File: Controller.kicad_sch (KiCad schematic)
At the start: 0 parts

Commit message: Add files via upload
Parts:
- added C1, C2, C3: 104, symbol Device:C_US
- added C4, C5: 22P, symbol Device:C_US
- added C6, C7: 12P, symbol Device:C_US
- added D4, D5, D6: LED, symbol Device:LED
- added J1: Conn_ARM_JTAG_SWD_20, symbol Connector:Conn_ARM_JTAG_SWD_20
- added J2: Conn_01x05_Pin, symbol Connector:Conn_01x05_Pin
- added J3, J6, J7: Conn_01x04_Pin, symbol Connector:Conn_01x04_Pin
- added J4, J9: Conn_01x02_Pin, symbol Connector:Conn_01x02_Pin
- added J5: Screw_Terminal_01x02, symbol Connector:Screw_Terminal_01x02
- added J8: Conn_01x06_Pin, symbol Connector:Conn_01x06_Pin
- added R1, R12, R2, R3, R4, R5, R6, R7, R8: 10K, symbol Device:R
- added R10, R11, R9: 510R, symbol Device:R
- added SW1, SW2: SW_Push, symbol Switch:SW_Push
- added U1: STM32F407VETx, Package_QFP:LQFP-100_14x14mm_P0.5mm, symbol MCU_ST_STM32F4:STM32F407VETx
- added U2: W25Q16JVSS, Package_SO:SOIC-8_5.3x5.3mm_P1.27mm, symbol Memory_Flash:W25Q16JVSS
- added U3: MAX485E, Package_SO:SOIC-8_3.9x4.9mm_P1.27mm, symbol Interface_UART:MAX485E
- added Y1: 8M, symbol Device:Crystal
- added Y2: 32.768K, symbol Device:Crystal
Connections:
- new net: R7.2, SW1.2, U1.94 (BOOT0)
- new net: R9.1, U1.15 (PC0)
- new net: D4.2 (A), R9.2
- new net: C4.1, R12.1, U1.12 (PH0), Y1.2
- new net: C5.1, R12.2, U1.13 (PH1), Y1.1
- new net: C7.1, U1.8 (PC14), Y2.1
- new net: C6.1, U1.9 (PC15), Y2.2
- new net: J5.1 (Pin_1), U3.6 (A)
- new net: J5.2 (Pin_2), U3.7 (B)
- new net: R10.1, U1.16 (PC1)
- new net: D5.2 (A), R10.2
- new net: U1.10 (VSS), U1.27 (VSS), U1.74 (VSS), U1.99 (VSS)
- new net: R11.1, U1.17 (PC2)
- new net: D6.2 (A), R11.2
- new net  F_CS PA7: R8.2, U2.1 (~{CS})
- new net +3V3: C1.1, C3.1, J1.1 (VTREF), J1.2 (VCC/NC), R1.1, R3.1, R4.1, R5.1, R6.1, R8.1, SW1.1, U2.3 (~{WP}/IO_{2}), U2.7 (~{HOLD}/~{RESET}/IO_{3}), U2.8 (VCC)
- new net +5V: U3.8 (VCC)
- new net 3V3: J2.4 (Pin_4), J3.4 (Pin_4)
- new net F_CS PA7: U1.32 (PA7)
- new net GND: C1.2, C2.2, C3.2, C4.2, C5.2, C6.2, C7.2, D4.1 (K), D5.1 (K), D6.1 (K), J1.10 (GND), J1.12 (GND), J1.14 (GND), J1.16 (GND), J1.18 (GND), J1.20 (GND), J1.4 (GND), J1.6 (GND), J1.8 (GND), J2.5 (Pin_5), J3.3 (Pin_3), J4.1 (Pin_1), R2.1, R7.1, SW2.1, U2.4 (GND), U3.5 (GND)
- new net PA0 (ADC123_IN0): J8.1 (Pin_1), U1.23 (PA0)
- new net PA1(ADC123_IN1): J8.2 (Pin_2), U1.24 (PA1)
- new net PA10(TIM1_CH3): J6.3 (Pin_3), U1.69 (PA10)
- new net PA11(TIM1_CH4): J6.4 (Pin_4), U1.70 (PA11)
- new net PA2(ADC123_IN2): J8.3 (Pin_3), U1.25 (PA2)
- new net PA3(ADC123_IN3): J8.4 (Pin_4), U1.26 (PA3)
- new net PA4(ADC123_IN4): J8.5 (Pin_5), J9.1 (Pin_1), U1.29 (PA4)
- new net PA8(TIM1_CH1): J6.1 (Pin_1), U1.67 (PA8)
- new net PA9(TIM1_CH2): J6.2 (Pin_2), U1.68 (PA9)
- new net PC6 (TIM8_CH1): J7.1 (Pin_1), U1.63 (PC6)
- new net PC7 (TIM8_CH2): J7.2 (Pin_2), U1.64 (PC7)
- new net PC8 (TIM8_CH3): J7.3 (Pin_3), U1.65 (PC8)
- new net PC9 (TIM8_CH4): J7.4 (Pin_4), U1.66 (PC9)
- new net RST: C2.1, J1.15 (~{SRST}), J2.3 (Pin_3), J4.2 (Pin_2), R6.2, SW2.2, U1.14 (NRST)
- new net RX (PA10): J3.2 (Pin_2)
- new net SPI1_MISO PA6: U1.31 (PA6), U2.2 (DO/IO_{1})
- new net SPI1_MOSI PA7: U2.5 (DI/IO_{0})
- new net SPI1_SCK PA5: J8.6 (Pin_6), J9.2 (Pin_2), U1.30 (PA5), U2.6 (CLK)
- new net SWCLK (PA14): J2.2 (Pin_2)
- new net SWDIO (PA13): J2.1 (Pin_1)
- new net TCK: J1.9 (TCK/SWCLK), R2.2, U1.76 (PA14)
- new net TDI: J1.5 (TDI), R4.2, U1.77 (PA15)
- new net TDO: J1.13 (TDO/SWO), R5.2, U1.89 (PB3)
- new net TMS: J1.7 (TMS/SWDIO), R3.2, U1.72 (PA13)
- new net TRST: J1.3 (~{TRST}), R1.2, U1.90 (PB4)
- new net TX (PA9): J3.1 (Pin_1)
- new net Tranciver DE: U1.33 (PC4), U3.3 (DE)
- new net Tranciver RE: U1.18 (PC3), U3.2 (~{RE})
- new net UART RX PA10: U3.4 (DI)
- new net UART TX PA9: U3.1 (RO)
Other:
- note added: "ADC pins"
- note added: "Button and needed circuitry for RESET"
- note added: "DAC pins"
- note added: "JTAG/SWD Debug Interface"
- note added: "Needed Headers for SWD debugging"
- note added: "Needed Headers for UART programming"
- note added: "Needed circuitry for flash"
- note added: "RS485 Tranciver"
- note added: "TIM1 pins"
- note added: "TIM8 pins"

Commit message: Latest updates
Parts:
- removed C1, C3: 104, symbol Device:C_US
- removed C6, C7: 12P, symbol Device:C_US
- removed D4, D5, D6: LED, symbol Device:LED
- removed J1: Conn_ARM_JTAG_SWD_20, symbol Connector:Conn_ARM_JTAG_SWD_20
- removed J2: Conn_01x05_Pin, symbol Connector:Conn_01x05_Pin
- removed J5: Screw_Terminal_01x02, symbol Connector:Screw_Terminal_01x02
- removed J6, J7: Conn_01x04_Pin, symbol Connector:Conn_01x04_Pin
- removed J8: Conn_01x06_Pin, symbol Connector:Conn_01x06_Pin
- removed J9: Conn_01x02_Pin, symbol Connector:Conn_01x02_Pin
- removed R1, R4, R8: 10K, symbol Device:R
- removed R10, R11, R9: 510R, symbol Device:R
- removed SW1: SW_Push, symbol Switch:SW_Push
- removed U2: W25Q16JVSS, Package_SO:SOIC-8_5.3x5.3mm_P1.27mm, symbol Memory_Flash:W25Q16JVSS
- removed U3: MAX485E, Package_SO:SOIC-8_3.9x4.9mm_P1.27mm, symbol Interface_UART:MAX485E
- added C10, C11, C12, C13, C23, C7, C8, C9: 100n, symbol Device:C
- added C14: 4.7u, symbol Device:C
- added C3, C4: 2.2u, symbol Device:C
- added C5, C6: 6.8p, symbol Device:C
- added D1, D2, D3: LED, symbol Device:LED
- added J12: Conn_01x03_Pin, symbol Connector:Conn_01x03_Pin
- added J2: Conn_01x04_Pin, symbol Connector:Conn_01x04_Pin
- added J3, J4: Conn_01x02_Pin, symbol Connector:Conn_01x02_Pin
- added R17, R6: 1k, symbol Device:R
- added U6: TL431M-0.3%-6AF, EasyEDA:SOT-23-3_L2.9-W1.6-P1.90-LS2.8-BR, symbol EasyEDA:TL431M-0.3%-6AF
- C1: renamed from C4; value 22P -> 20p
- C15: renamed from C2; value 104 -> 1u
- C2: renamed from C5; value 22P -> 20p
- R5, R7: value 10K -> 1k
- renumbered J3 to J5, J4 to J6, R12 to R1, R6 to R4, SW2 to SW1
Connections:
- net 3V3 is gone; now on net GND: J5.4 (Pin_4)
- net RX (PA10) is gone; now on net UART1_Rx: J5.2 (Pin_2)
- net TX (PA9) is gone; now on net UART1_Tx: J5.1 (Pin_1)
- net +3V3: now also J5.3 (Pin_3), U1.100 (VDD), U1.11 (VDD), U1.19 (VDD), U1.22 (VDDA), U1.28 (VDD), U1.50 (VDD), U1.75 (VDD), C10.1, C11.1, C12.1, C13.1, C14.1, C7.1, C8.1, C9.1, D1.1 (K), D2.1 (K), D3.1 (K), J12.3 (Pin_3), J2.3 (Pin_3), J3.2 (Pin_2), J4.2 (Pin_2), R17.1; no longer R3.1, R5.1
- net GND: now also R2.2, R3.2, U1.10 (VSS), U1.20 (VSSA), U1.27 (VSS), U1.74 (VSS), U1.99 (VSS), C10.2, C11.2, C12.2, C13.2, C14.2, C23.2, C3.2, C4.2, C5.2, C6.2, C7.2, C8.2, C9.2, J2.4 (Pin_4), U6.3 (A); no longer J5.3 (Pin_3), R2.1, R7.1
- net SWCLK (PA14): now also U1.76 (PA14), J2.2 (Pin_2)
- net SWDIO (PA13): now also U1.72 (PA13), J2.1 (Pin_1)
- net at R7.2: now also D3.2 (A); no longer U1.94 (BOOT0)
- net UserLED1: now reaches U1.15 (PC0)
- net UserLED1: now also R5.1
- net at U1.8 (PC14), Y2.1: now also C5.1
- net at U1.9 (PC15), Y2.2: now also C6.1
- net UserLED2: now reaches U1.16 (PC1)
- net UserLED2: now also R6.1
- net UserLED3: now reaches U1.17 (PC2)
- net UserLED3: now also R7.1
- net VREF: now reaches U1.21 (VREF+)
- net VREF: now also C23.1, J12.2 (Pin_2)
- net BOOT1: now reaches U1.37 (PB2)
- net BOOT1: now also R2.1, J3.1 (Pin_1)
- net at U1.49 (VCAP_1): now also C3.1
- net PB13(TIM1_CH1N): now reaches U1.52 (PB13)
- net PB14(TIM1_CH2N): now reaches U1.53 (PB14)
- net PB15(TIM1_CH3N): now reaches U1.54 (PB15)
- net OTG_FS_DP: now reaches U1.71 (PA12)
- net at U1.73 (VCAP_2): now also C4.1
- net UART1_Tx: now reaches U1.92 (PB6)
- net UART1_Rx: now reaches U1.93 (PB7)
- net CAN1_Rx: now reaches U1.95 (PB8)
- net CAN1_Tx: now reaches U1.96 (PB9)
- net F_CS PA7: no longer names the net of U1.32 (PA7)
- net PA0 (ADC123_IN0): no longer names the net of U1.23 (PA0)
- net PA1(ADC123_IN1): no longer names the net of U1.24 (PA1)
- net PA11(TIM1_CH4) renamed OTG_FS_DM
- net PA2(ADC123_IN2) renamed UART2_Tx
- net PA3(ADC123_IN3) renamed UART2_Rx
- net PA4(ADC123_IN4): no longer names the net of U1.29 (PA4)
- net PC6 (TIM8_CH1): no longer names the net of U1.63 (PC6)
- net PC7 (TIM8_CH2): no longer names the net of U1.64 (PC7)
- net PC8 (TIM8_CH3): no longer names the net of U1.65 (PC8)
- net PC9 (TIM8_CH4): no longer names the net of U1.66 (PC9)
- net RST renamed NRST
- net SPI1_MISO PA6: no longer names the net of U1.31 (PA6)
- net SPI1_SCK PA5: no longer names the net of U1.30 (PA5)
- removed net TCK: R2.2, U1.76 (PA14)
- net TDI: no longer names the net of U1.77 (PA15)
- net TDO: no longer names the net of U1.89 (PB3)
- net TDO: no longer R5.2
- removed net TMS: R3.2, U1.72 (PA13)
- net TRST: no longer names the net of U1.90 (PB4)
- net Tranciver DE: no longer names the net of U1.33 (PC4)
- net Tranciver RE: no longer names the net of U1.18 (PC3)
- new net: D2.2 (A), R6.2
- new net: D1.2 (A), R5.2
- new net BOOT0: J4.1 (Pin_1), R3.1, U1.94 (BOOT0)
- new net VREF_2.5V: J12.1 (Pin_1), R17.2, U6.1 (REF), U6.2 (C)
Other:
- note added: "HSE and LSE circuitry based on https://github.com/AlexanderDev/stm32f4discovery/blob/master/doc/schematics.pdf"
- note added: "Needed Headers for UART programming/Debugging"
- note added: "USER LEDS"
- note removed: "ADC pins"
- note removed: "DAC pins"
- note removed: "JTAG/SWD Debug Interface"
- note removed: "Needed Headers for UART programming"
- note removed: "Needed circuitry for flash"
- note removed: "RS485 Tranciver"
- note removed: "TIM1 pins"
- note removed: "TIM8 pins"
- moved on the sheet: C1, C15, C2, J5, J6, R1, R4, SW1, U1, Y1, Y2

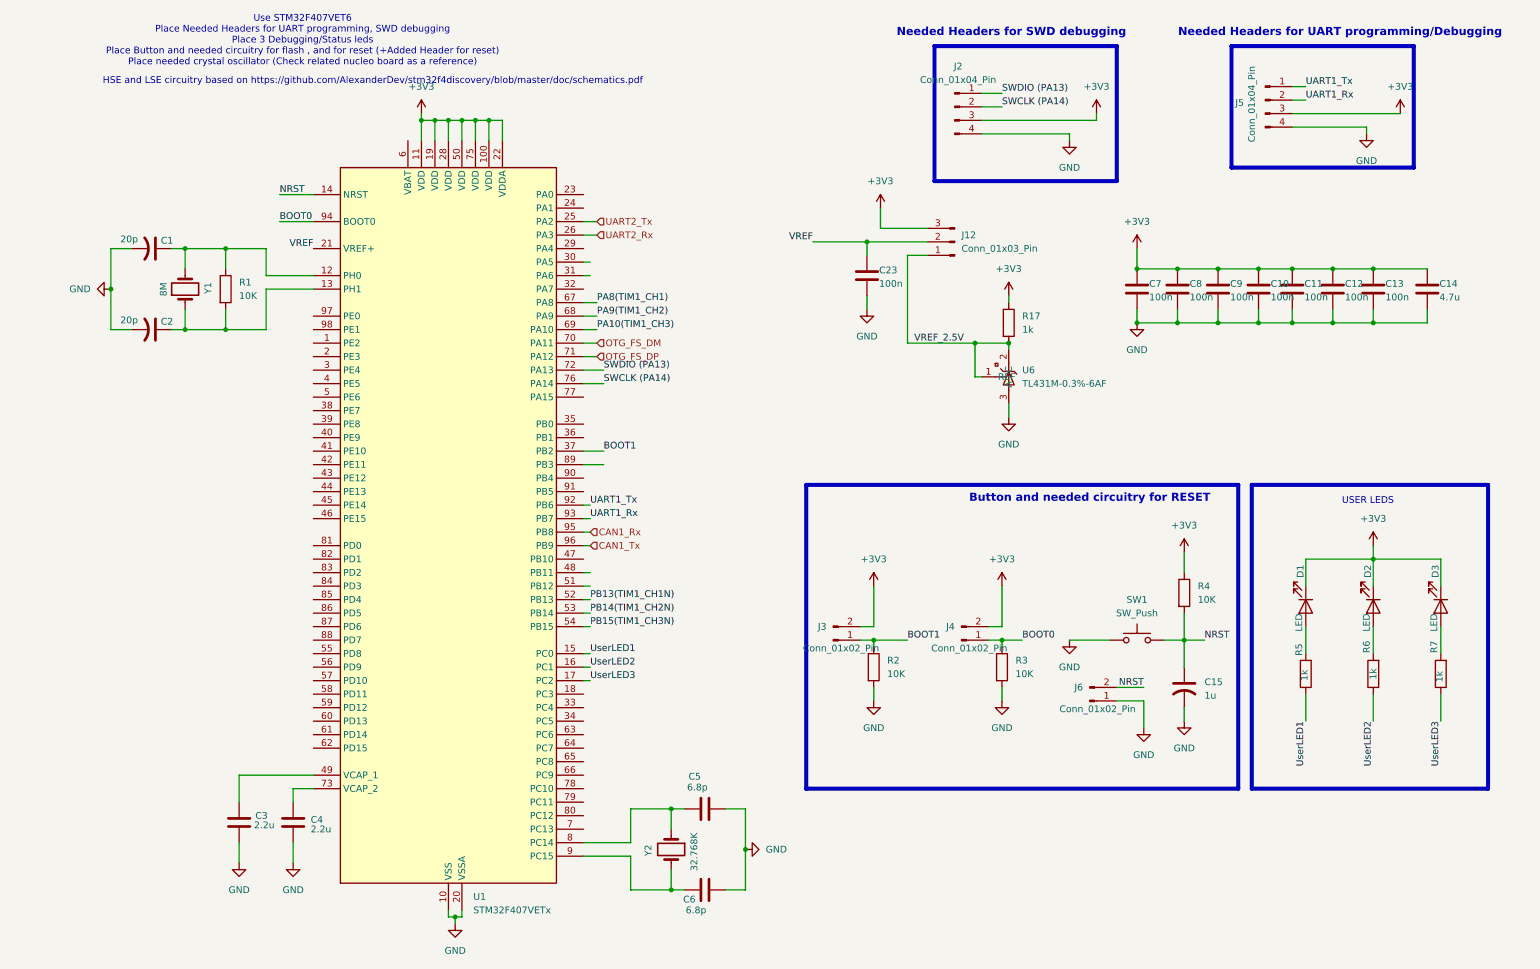
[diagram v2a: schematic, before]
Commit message: Latest changes (added SD , USB , CAN , RS485)
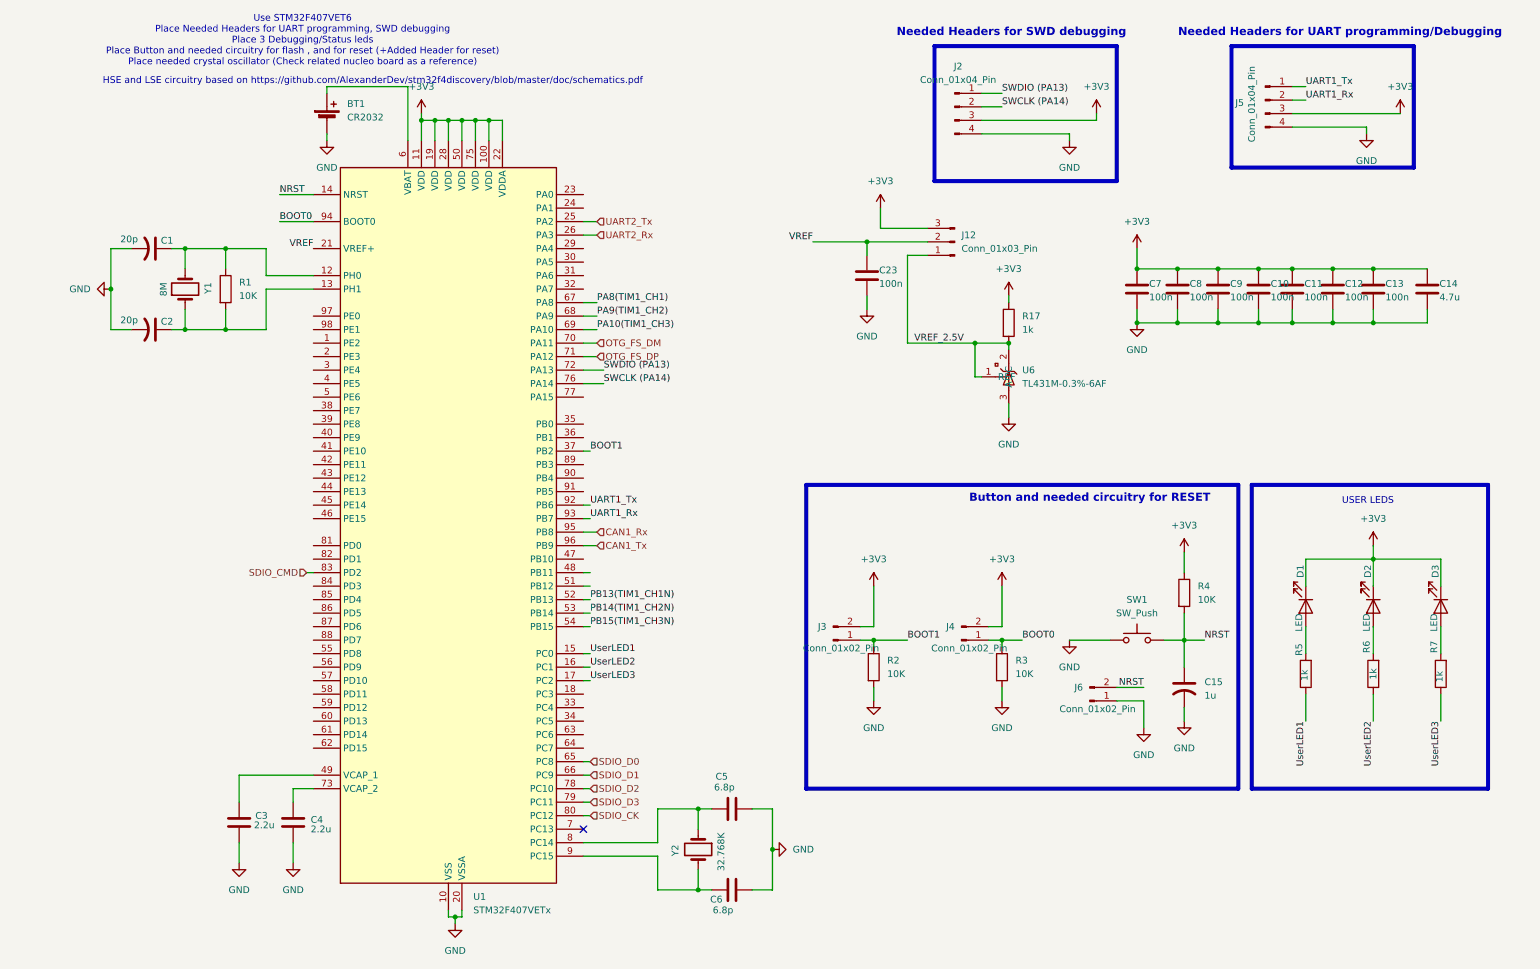
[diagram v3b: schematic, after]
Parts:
- added BT1: CR2032, EasyEDA:BAT_1074, symbol Device:Battery_Cell
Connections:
- net GND: now also BT1.2 (-)
- net at U1.6 (VBAT): now also BT1.1 (+)
- net SDIO_D0: now reaches U1.65 (PC8)
- net SDIO_D1: now reaches U1.66 (PC9)
- net SDIO_D2: now reaches U1.78 (PC10)
- net SDIO_D3: now reaches U1.79 (PC11)
- net SDIO_CK: now reaches U1.80 (PC12)
- net SDIO_CMD: now reaches U1.83 (PD2)
- no-connect marks 0 -> 1
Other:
- moved on the sheet: C5, C6, Y2

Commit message: added Ethernet and SPI interface
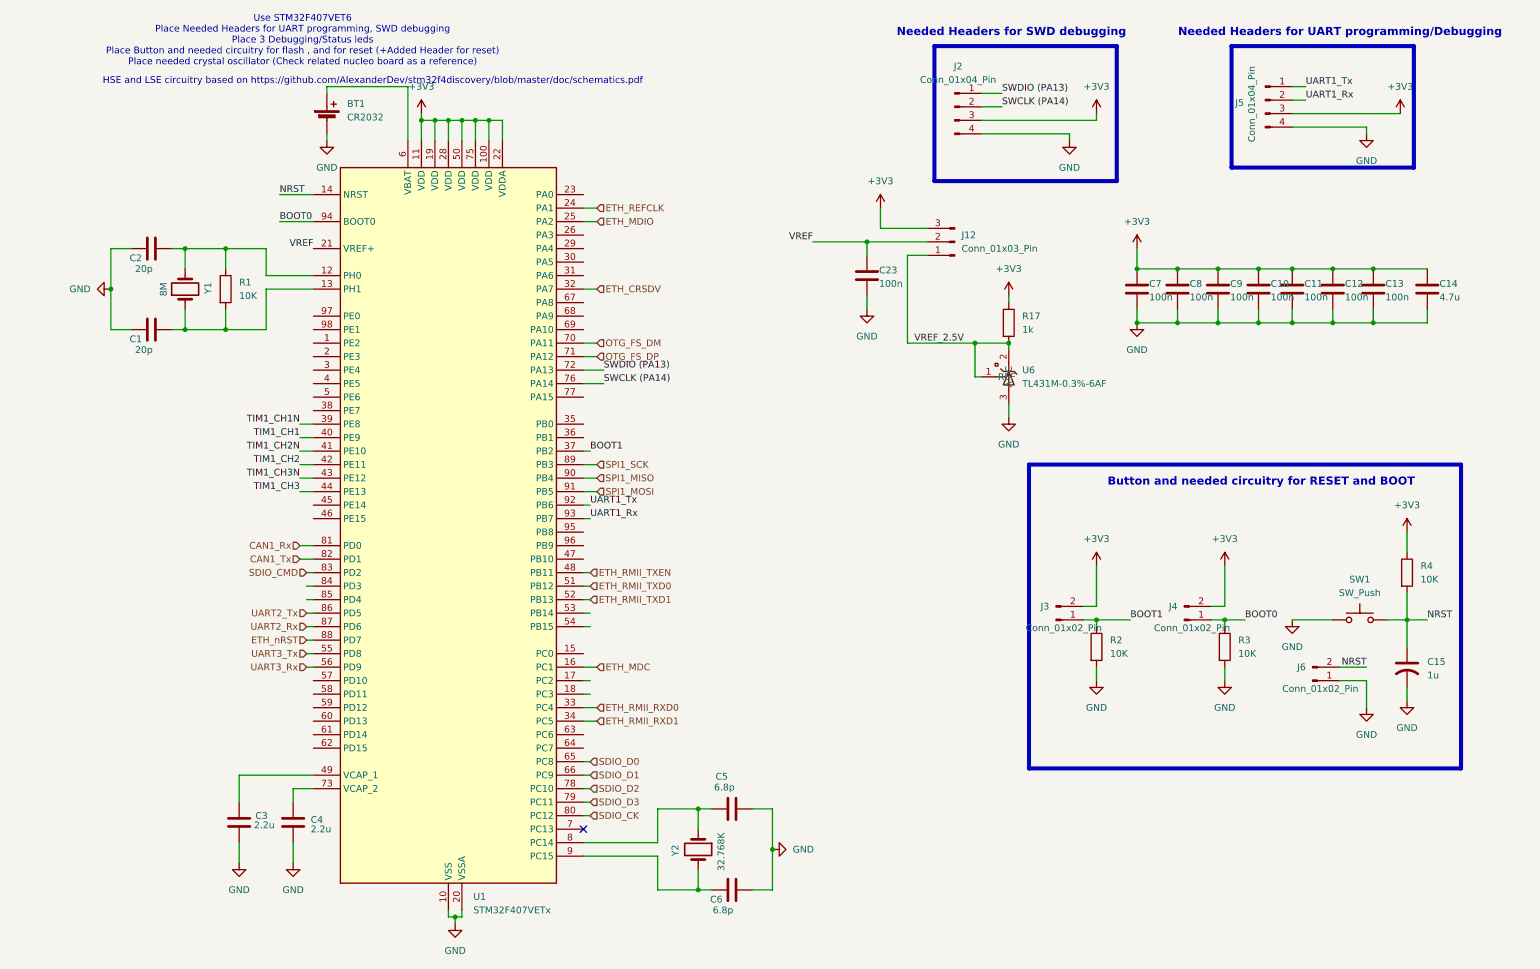
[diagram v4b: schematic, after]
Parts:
- removed C1, C2: 20p, symbol Device:C_US
- removed D1, D2, D3: LED, symbol Device:LED
- removed R5, R6, R7: 1k, symbol Device:R
- added C1, C2: 20p, symbol Device:C
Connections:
- net CAN1_Rx: now also U1.81 (PD0); no longer U1.95 (PB8)
- net CAN1_Tx: now also U1.82 (PD1); no longer U1.96 (PB9)
- net GND: now also C1.1, C2.1
- net UART2_Rx: now also U1.87 (PD6); no longer U1.26 (PA3)
- net UART2_Tx: now also U1.86 (PD5); no longer U1.25 (PA2)
- net at R1.1, U1.12 (PH0), Y1.2: now also C2.2
- net at R1.2, U1.13 (PH1), Y1.1: now also C1.2
- net ETH_REFCLK: now reaches U1.24 (PA1)
- net ETH_CRSDV: now reaches U1.32 (PA7)
- net ETH_RMII_RXD0: now reaches U1.33 (PC4)
- net ETH_RMII_RXD1: now reaches U1.34 (PC5)
- net TIM1_CH1N: now reaches U1.39 (PE8)
- net TIM1_CH1: now reaches U1.40 (PE9)
- net TIM1_CH2N: now reaches U1.41 (PE10)
- net TIM1_CH2: now reaches U1.42 (PE11)
- net TIM1_CH3N: now reaches U1.43 (PE12)
- net TIM1_CH3: now reaches U1.44 (PE13)
- net ETH_RMII_TXEN: now reaches U1.48 (PB11)
- net ETH_RMII_TXD0: now reaches U1.51 (PB12)
- net UART3_Tx: now reaches U1.55 (PD8)
- net UART3_Rx: now reaches U1.56 (PD9)
- net ETH_nRST: now reaches U1.88 (PD7)
- net SPI1_SCK: now reaches U1.89 (PB3)
- net SPI1_MISO: now reaches U1.90 (PB4)
- net SPI1_MOSI: now reaches U1.91 (PB5)
- net PA10(TIM1_CH3): no longer names the net of U1.69 (PA10)
- net PA8(TIM1_CH1): no longer names the net of U1.67 (PA8)
- net PA9(TIM1_CH2): no longer names the net of U1.68 (PA9)
- net PB13(TIM1_CH1N) renamed ETH_RMII_TXD1
- net PB14(TIM1_CH2N): no longer names the net of U1.53 (PB14)
- net PB15(TIM1_CH3N): no longer names the net of U1.54 (PB15)
- net UserLED1: no longer names the net of U1.15 (PC0)
- net UserLED2 renamed ETH_MDC
- net UserLED3: no longer names the net of U1.17 (PC2)
- new net ETH_MDIO: U1.25 (PA2)
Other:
- note added: "Button and needed circuitry for RESET and BOOT"
- note removed: "Button and needed circuitry for RESET"
- note removed: "USER LEDS"
- moved on the sheet: C15, J3, J4, J6, R2, R3, R4, SW1
